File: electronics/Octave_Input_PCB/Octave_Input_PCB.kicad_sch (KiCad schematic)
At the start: 66 parts, among them J1 HRO_TYPE-C-31-M-12, SW1 SW_Hot_Swap_Socket, SW10 SW_Hot_Swap_Socket, SW11 SW_Hot_Swap_Socket, SW12 SW_Hot_Swap_Socket, SW13 SW_Hot_Swap_Socket, SW14 Alps_Alpine_RKJXV1224, SW15 Bourns_PEC12R-4xxxF-Sxxx, SW2 SW_Hot_Swap_Socket, SW21 Alps_Alpine_SKRP, SW22 Alps_Alpine_SKRP, SW3 SW_Hot_Swap_Socket, SW4 SW_Hot_Swap_Socket, SW5 SW_Hot_Swap_Socket, SW6 SW_Hot_Swap_Socket, SW7 SW_Hot_Swap_Socket, SW8 SW_Hot_Swap_Socket, SW9 SW_Hot_Swap_Socket, U1 AP2112K-3.3, U2 Raspberry_Pi_RP2040, U3 W25Q64JVSS, Y1 12MHz

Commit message: [WIP] Update schematic and PCB
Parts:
- removed C21, C22: 0.01u, Octave_Library:C_0805_2012Metric, symbol Device:C
- removed R11, R13: 100K, Octave_Library:R_0805_2012Metric, symbol Device:R_US
- removed R12, R14: 10K, Octave_Library:R_0805_2012Metric, symbol Device:R_US
- added C21, C22: 0.01uF, Capacitor_SMD:C_0402_1005Metric, symbol Device:C_Small
- added R11, R13: 100K, Resistor_SMD:R_0402_1005Metric, symbol Device:R_Small
- added R12, R14: 10K, Resistor_SMD:R_0402_1005Metric, symbol Device:R_Small
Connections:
- net +3V3: now also R11.1, R13.1
- net A: now also C22.1, R14.1
- net B: now also C21.1, R12.2
- net GND: now also C21.2, C22.2
- net SignalA: now also R13.2, R14.2
- net SignalB: now also R11.2, R12.1

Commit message: [WIP] Update schematic and PCB
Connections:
- net SignalA is gone; now on net rotaryA: R13.2, R14.2
- net SignalB is gone; now on net rotaryB: R11.2, R12.1
- net col0: now also U2.34 (GPIO22)
- net col1: now also SW14.1, U2.35 (GPIO23)
- net col2: now also U2.2 (GPIO0); no longer SW14.1
- net col3: now also U2.3 (GPIO1)
- net row0: now also U2.41 (GPIO29/ADC3)
- net row1: now also U2.40 (GPIO28/ADC2)
- net row2: now also U2.37 (GPIO25)
- net row3: now also U2.36 (GPIO24)
- net NEOPIX_POWER: now reaches U2.14 (GPIO11)
- net NEOPIX: now reaches U2.15 (GPIO12)
- net stickA: now reaches U2.38 (GPIO26/ADC0)
- net stickA: now also SW14.4
- net stickB: now reaches U2.39 (GPIO27/ADC1)
- net stickB: now also SW14.7
- net rotaryA: now reaches U2.4 (GPIO2)
- net rotaryB: now reaches U2.5 (GPIO3)
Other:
- moved on the sheet: D14, SW14

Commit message: [WIP] Update schematic and PCB
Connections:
- net row0: now also U2.37 (GPIO25); no longer U2.41 (GPIO29/ADC3)
- net row2: now also U2.41 (GPIO29/ADC3); no longer U2.37 (GPIO25)
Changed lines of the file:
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@@
     )
   )
-  (global_label "row0" (shape input) (at 114.3 182.88 0) (fields_autoplaced)
+  (global_label "row0" (shape input) (at 114.3 170.18 0) (fields_autoplaced)
     (effects (font (size 1.27 1.27)) (justify left))
-    (property "Intersheet References" "${INTERSHEET_REFS}" (id 0) (at 121.1883 182.8006 0)
+    (property "Intersheet References" "${INTERSHEET_REFS}" (id 0) (at 121.1883 170.1006 0)
       (effects (font (size 1.27 1.27)) (justify left) hide)
     )
@@
     )
   )
-  (global_label "row2" (shape input) (at 114.3 170.18 0) (fields_autoplaced)
+  (global_label "row2" (shape input) (at 114.3 182.88 0) (fields_autoplaced)
     (effects (font (size 1.27 1.27)) (justify left))
-    (property "Intersheet References" "${INTERSHEET_REFS}" (id 0) (at 121.1883 170.1006 0)
+    (property "Intersheet References" "${INTERSHEET_REFS}" (id 0) (at 121.1883 182.8006 0)
       (effects (font (size 1.27 1.27)) (justify left) hide)
     )

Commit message: [WIP] Update schematic and PCB
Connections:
- net col0: now also U2.36 (GPIO24); no longer U2.34 (GPIO22)
- net row3: now also U2.34 (GPIO22); no longer U2.36 (GPIO24)
- net stickA: now also U2.39 (GPIO27/ADC1); no longer U2.38 (GPIO26/ADC0)
- net stickB: now also U2.38 (GPIO26/ADC0); no longer U2.39 (GPIO27/ADC1)
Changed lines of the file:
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@@
   (title_block
     (title "Octave - Input PCB")
-    (date "2022-05-25")
+    (date "2022-05-28")
     (rev "5.a")
     (comment 4 "https://github.com/takayoshiotake/octave-12-key-macropad")
@@
     )
   )
-  (global_label "row3" (shape input) (at 114.3 167.64 0) (fields_autoplaced)
-    (effects (font (size 1.27 1.27)) (justify left))
-    (property "Intersheet References" "${INTERSHEET_REFS}" (id 0) (at 121.1883 167.5606 0)
+  (global_label "row3" (shape input) (at 114.3 162.56 0) (fields_autoplaced)
+    (effects (font (size 1.27 1.27)) (justify left))
+    (property "Intersheet References" "${INTERSHEET_REFS}" (id 0) (at 121.1883 162.4806 0)
       (effects (font (size 1.27 1.27)) (justify left) hide)
     )
@@
     )
   )
-  (global_label "stickA" (shape input) (at 114.3 175.26 0) (fields_autoplaced)
-    (effects (font (size 1.27 1.27)) (justify left))
-    (property "Intersheet References" "${INTERSHEET_REFS}" (id 0) (at 122.2769 175.1806 0)
+  (global_label "stickA" (shape input) (at 114.3 177.8 0) (fields_autoplaced)
+    (effects (font (size 1.27 1.27)) (justify left))
+    (property "Intersheet References" "${INTERSHEET_REFS}" (id 0) (at 122.2769 177.7206 0)
       (effects (font (size 1.27 1.27)) (justify left) hide)
     )
@@
     )
   )
-  (global_label "col0" (shape input) (at 114.3 162.56 0) (fields_autoplaced)
-    (effects (font (size 1.27 1.27)) (justify left))
-    (property "Intersheet References" "${INTERSHEET_REFS}" (id 0) (at 120.8255 162.4806 0)
+  (global_label "col0" (shape input) (at 114.3 167.64 0) (fields_autoplaced)
+    (effects (font (size 1.27 1.27)) (justify left))
+    (property "Intersheet References" "${INTERSHEET_REFS}" (id 0) (at 120.8255 167.5606 0)
       (effects (font (size 1.27 1.27)) (justify left) hide)
     )
@@
     )
   )
-  (global_label "stickB" (shape input) (at 114.3 177.8 0) (fields_autoplaced)
-    (effects (font (size 1.27 1.27)) (justify left))
-    (property "Intersheet References" "${INTERSHEET_REFS}" (id 0) (at 122.4583 177.7206 0)
-      (effects (font (size 1.27 1.27)) (justify left) hide)
-    )
+  (global_label "stickB" (shape input) (at 114.3 175.26 0) (fields_autoplaced)
+    (effects (font (size 1.27 1.27)) (justify left))
+    (property "Intersheet References" "${INTERSHEET_REFS}" (id 0) (at 122.4583 175.1806 0)
+      (effects (font (size 1.27 1.27)) (justify left) hide)
+    )

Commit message: Update schematic and PCB
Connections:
- net rotaryA: now also U2.5 (GPIO3); no longer U2.4 (GPIO2)
- net rotaryB: now also U2.4 (GPIO2); no longer U2.5 (GPIO3)
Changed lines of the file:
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@@
     )
   )
-  (global_label "rotaryA" (shape input) (at 114.3 106.68 0) (fields_autoplaced)
+  (global_label "rotaryA" (shape input) (at 114.3 109.22 0) (fields_autoplaced)
     (effects (font (size 1.27 1.27)) (justify left))
-    (property "Intersheet References" "${INTERSHEET_REFS}" (id 0) (at 123.3655 106.7594 0)
+    (property "Intersheet References" "${INTERSHEET_REFS}" (id 0) (at 123.3655 109.2994 0)
       (effects (font (size 1.27 1.27)) (justify left) hide)
     )
@@
     )
   )
-  (global_label "rotaryB" (shape input) (at 114.3 109.22 0) (fields_autoplaced)
+  (global_label "rotaryB" (shape input) (at 114.3 106.68 0) (fields_autoplaced)
     (effects (font (size 1.27 1.27)) (justify left))
-    (property "Intersheet References" "${INTERSHEET_REFS}" (id 0) (at 123.5469 109.1406 0)
+    (property "Intersheet References" "${INTERSHEET_REFS}" (id 0) (at 123.5469 106.6006 0)
       (effects (font (size 1.27 1.27)) (justify left) hide)
     )

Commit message: Complete schematic and PCB (rev.5.0.0)
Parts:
- added LED1: WS2812C-2020-V1, Octave_Library:WS2812C-2020, symbol LED:WS2812B
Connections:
- net GND: now also LED1.3 (VSS)
- net NEOPIX: now also LED1.4 (DIN)
- net NEOPIX_POWER: now also LED1.1 (VDD)
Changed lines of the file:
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@@
   (title_block
     (title "Octave - Input PCB")
-    (date "2022-05-28")
-    (rev "5.a")
+    (date "2022-05-29")
+    (rev "5.0.0")
     (comment 4 "https://github.com/takayoshiotake/octave-12-key-macropad")
   )
@@
     (stroke (width 0) (type default) (color 0 0 0 0))
   )
+  (wire (pts (xy 149.86 124.46) (xy 152.4 124.46))
+    (stroke (width 0) (type default) (color 0 0 0 0))
+  )
   (wire (pts (xy 48.26 40.64) (xy 50.8 40.64))
     (stroke (width 0) (type default) (color 0 0 0 0))
@@
   )
   (wire (pts (xy 233.68 33.02) (xy 233.68 48.26))
+    (stroke (width 0) (type default) (color 0 0 0 0))
+  )
+  (wire (pts (xy 152.4 124.46) (xy 152.4 127))
     (stroke (width 0) (type default) (color 0 0 0 0))
   )
@@
     )
   )
+  (global_label "NEOPIX" (shape input) (at 144.78 134.62 180) (fields_autoplaced)
+    (effects (font (size 1.27 1.27)) (justify right))
+    (property "Intersheet References" "${INTERSHEET_REFS}" (id 0) (at 135.4726 134.6994 0)
+      (effects (font (size 1.27 1.27)) (justify right) hide)
+    )
+  )
   (global_label "D+" (shape input) (at 48.26 134.62 180) (fields_autoplaced)
     (effects (font (size 1.27 1.27)) (justify right))
@@
     )
   )
+  (global_label "NEOPIX_POWER" (shape input) (at 149.86 124.46 180) (fields_autoplaced)
+    (effects (font (size 1.27 1.27)) (justify right))
+    (property "Intersheet References" "${INTERSHEET_REFS}" (id 0) (at 133.114 124.5394 0)
+      (effects (font (size 1.27 1.27)) (justify right) hide)
+    )
+  )
   (global_label "B" (shape input) (at 261.62 88.9 270) (fields_autoplaced)
     (effects (font (size 1.27 1.27)) (justify right))
@@
     (pin "1")
     (pin "2")
+  )
+  (symbol (lib_id "power:GND") (at 152.4 142.24 0) (unit 1)
+    (in_bom yes) (on_board yes) (fields_autoplaced)
+    (property "Reference" "#PWR0144" (id 0) (at 152.4 148.59 0)
+      (effects (font (size 1.27 1.27)) hide)
+    )
+    (property "Value" "GND" (id 1) (at 152.4 147.32 0)
+      (effects (font (size 1.27 1.27)) hide)
+    )
+    (property "Footprint" "" (id 2) (at 152.4 142.24 0)
+      (effects (font (size 1.27 1.27)) hide)
+    )
+    (property "Datasheet" "" (id 3) (at 152.4 142.24 0)
+      (effects (font (size 1.27 1.27)) hide)
+    )
+    (pin "1")
   )
   (symbol (lib_id "Diode:1N4148WS") (at 226.06 36.83 90) (unit 1)
@@
     (pin "1")
   )
+  (symbol (lib_id "LED:WS2812B") (at 152.4 134.62 0) (unit 1)
+    (in_bom yes) (on_board yes) (fields_autoplaced)
+    (property "Reference" "LED1" (id 0) (at 168.91 130.2893 0))
+    (property "Value" "WS2812C-2020-V1" (id 1) (at 168.91 132.8293 0))
+    (property "Footprint" "Octave_Library:WS2812C-2020" (id 2) (at 153.67 142.24 0)
+      (effects (font (size 1.27 1.27)) (justify left top) hide)
+    )
+    (property "Datasheet" "" (id 3) (at 154.94 144.145 0)
+      (effects (font (size 1.27 1.27)) (justify left top) hide)
+    )
+    (pin "1")
+    (pin "2")
+    (pin "3")
+    (pin "4")
+  )
   (symbol (lib_id "power:+1V1") (at 68.58 88.9 0) (unit 1)
     (in_bom yes) (on_board yes)
@@
       (reference "#PWR0143") (unit 1) (value "GND") (footprint "")
     )
+    (path "/17a714e6-bc0f-4e80-93e3-5c3d6cd28b12"
+      (reference "#PWR0144") (unit 1) (value "GND") (footprint "")
+    )
     (path "/b4a74826-80b4-490c-898e-4ec787ca4628"
       (reference "C1") (unit 1) (value "1uF") (footprint "Capacitor_SMD:C_0402_1005Metric")
@@
       (reference "J1") (unit 1) (value "HRO_TYPE-C-31-M-12") (footprint "Octave_Library:HRO_TYPE-C-31-M-12")
     )
+    (path "/fb4a6e36-e345-48c2-af3e-c05b4dd8655d"
+      (reference "LED1") (unit 1) (value "WS2812C-2020-V1") (footprint "Octave_Library:WS2812C-2020")
+    )
     (path "/575bc9c1-f53b-4dee-b3d5-6bbc484509fa"

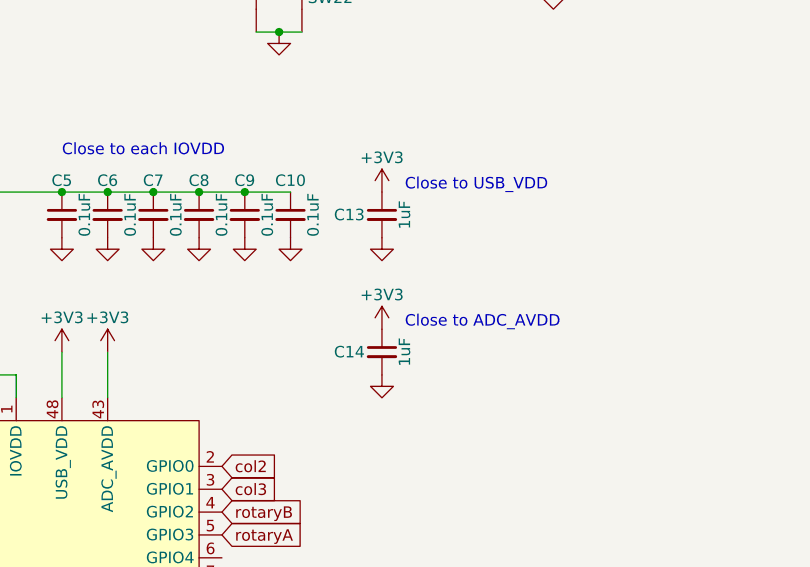
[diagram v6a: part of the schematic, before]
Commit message: Fix C13 and C14 value, improve Y1 pattern
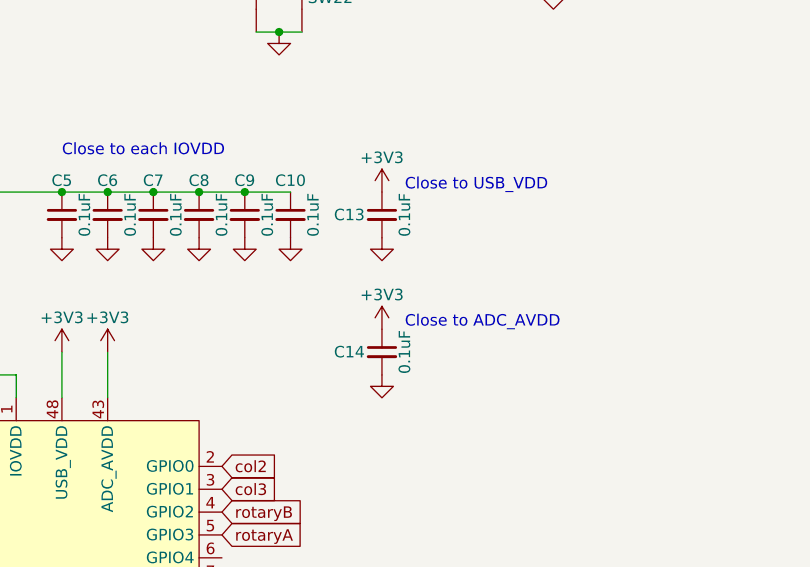
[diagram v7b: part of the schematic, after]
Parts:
- C13, C14: value 1uF -> 0.1uF
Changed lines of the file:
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@@
   (title_block
     (title "Octave - Input PCB")
-    (date "2022-05-29")
-    (rev "5.0.0")
+    (date "2022-05-30")
+    (rev "5.0.1")
     (comment 4 "https://github.com/takayoshiotake/octave-12-key-macropad")
   )
@@
       (effects (font (size 1.27 1.27)) (justify right))
     )
-    (property "Value" "1uF" (id 1) (at 134.62 73.66 90))
+    (property "Value" "0.1uF" (id 1) (at 134.62 73.66 90))
     (property "Footprint" "Capacitor_SMD:C_0402_1005Metric" (id 2) (at 132.08 73.66 0)
       (effects (font (size 1.27 1.27)) hide)
@@
       (effects (font (size 1.27 1.27)) (justify right))
     )
-    (property "Value" "1uF" (id 1) (at 134.62 88.9 90))
+    (property "Value" "0.1uF" (id 1) (at 134.62 88.9 90))
     (property "Footprint" "Capacitor_SMD:C_0402_1005Metric" (id 2) (at 132.08 88.9 0)
       (effects (font (size 1.27 1.27)) hide)
@@
     )
     (path "/3aa4ed2e-ad1e-405a-9597-e0bca0667af2"
-      (reference "C13") (unit 1) (value "1uF") (footprint "Capacitor_SMD:C_0402_1005Metric")
+      (reference "C13") (unit 1) (value "0.1uF") (footprint "Capacitor_SMD:C_0402_1005Metric")
     )
     (path "/9034adba-36c6-424f-8894-f569b3d72c53"
-      (reference "C14") (unit 1) (value "1uF") (footprint "Capacitor_SMD:C_0402_1005Metric")
+      (reference "C14") (unit 1) (value "0.1uF") (footprint "Capacitor_SMD:C_0402_1005Metric")
     )
     (path "/f49a4c76-450b-4d80-9ba7-af728063e684"
